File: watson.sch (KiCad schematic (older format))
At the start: 44 parts, among them P1 CONN_1, P2 CONN_1, P3 CONN_1, P4 CONN_1, P5 BNC, P6 CONN_1, U1 78L05, U2 79L05, U4 AD603, U5 AD8307

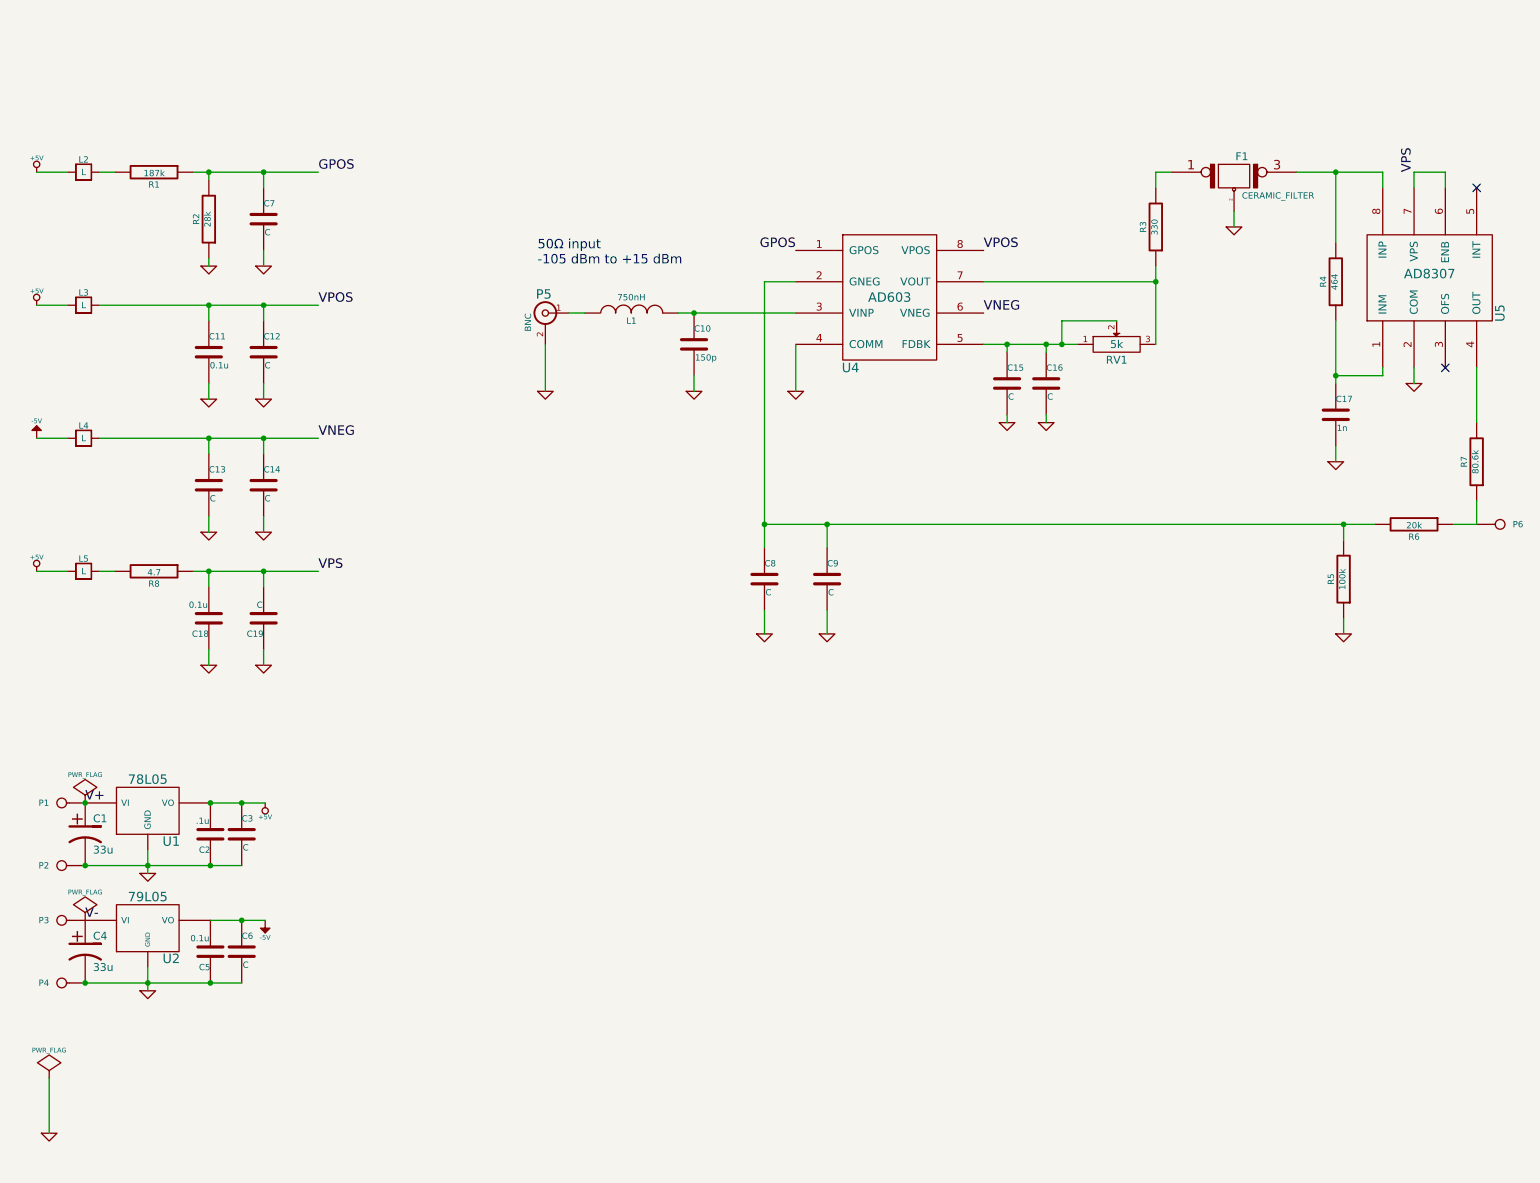
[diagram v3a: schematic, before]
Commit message: Added AD8031 to buffer output of AD8307.
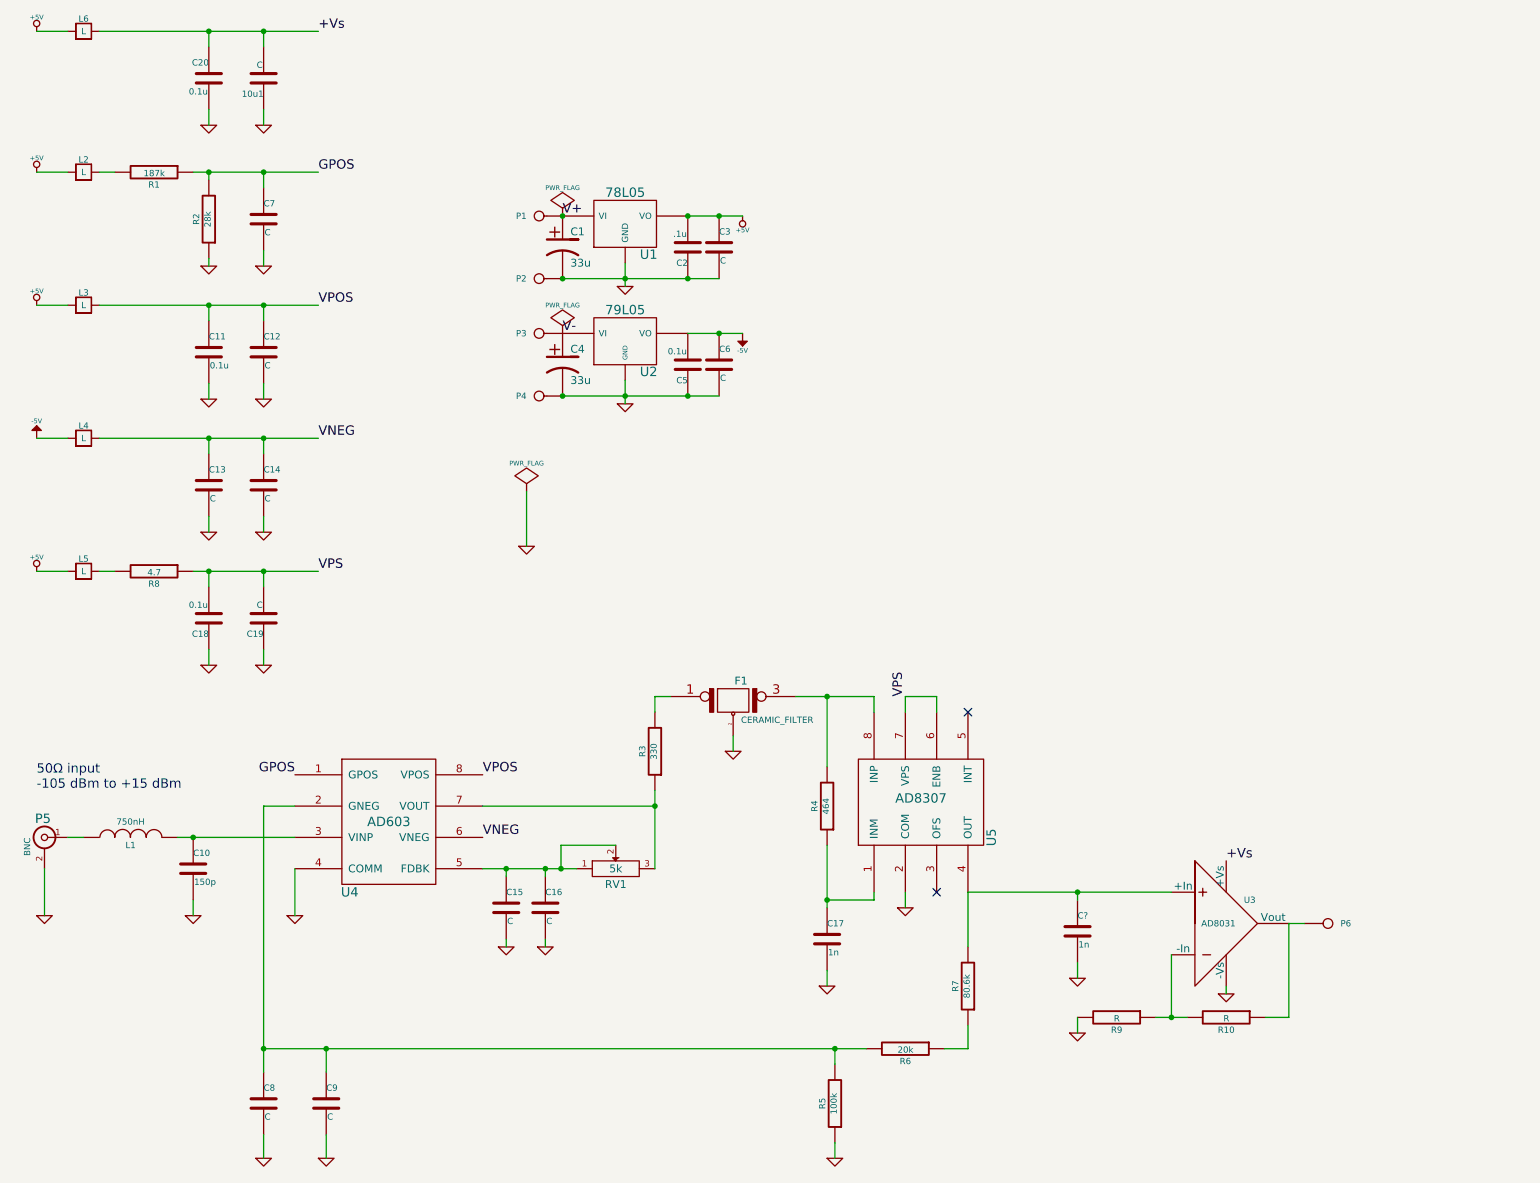
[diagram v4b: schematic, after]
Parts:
- added 10u1: C, ~, symbol C
- added C20: 0.1u, ~, symbol C
- added C?: 1n, ~, symbol C
- added L6: L, ~, symbol L
- added R10, R9: R, ~, symbol R
- added U3: AD8031, ~, symbol AD8031
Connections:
- net +5V: now also L6.1
- net GND: now also 10u1.1, C20.2, C?.2, R9.2, U3.2 (-Vs)
- net at R7.2, U5.4 (OUT): now also C?.1, U3.3 (+In)
- net at R6.1, R7.1: no longer P6.1
- new net: P6.1, R10.1, U3.1 (Vout)
- new net: R10.2, R9.1, U3.4 (-In)
- new net +Vs: 10u1.2, C20.1, L6.2, U3.5 (+Vs)
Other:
- moved on the sheet: C1, C10, C15, C16, C17, C2, C3, C4, C5, C6, C8, C9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

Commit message: This is the initial manufactured version of Watson, Watson 10 to be exact.
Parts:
- removed 10u1: C, ~, symbol C
- added C21: Spare, ~, symbol C
- C12, C14, C19, C7: value C -> Spare
- gave numbers to parts that had none: 1
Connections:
- net +Vs: now also C21.1
- net GND: now also C18.2, C19.2, C21.2; no longer C18.1, C19.1
- net VPS: now also C18.1, C19.1; no longer C18.2, C19.2
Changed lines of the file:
@@
-EESchema Schematic File Version 2  date Sunday, September 29, 2013 01:00:13 PM
+EESchema Schematic File Version 2  date Thursday, October 03, 2013 09:14:34 PM
 LIBS:watson
 LIBS:watson-cache
@@
 Sheet 1 1
 Title "Watson - A 10.7 MHz Power Meter"
-Date "29 sep 2013"
+Date "4 oct 2013"
 Rev "A"
 Comp "Copyright 2013 - Pare Technologies"
@@
 F 3 "~" H 1950 3650 60  0000 C CNN
 	1    1950 3650
-	-1   0    0    1
+	1    0    0    -1
 $EndComp
 $Comp
@@
 P 2300 2800
 F 0 "C14" H 2300 2900 40  0000 L CNN
-F 1 "C" H 2306 2715 40  0000 L CNN
+F 1 "Spare" H 2306 2715 40  0000 L CNN
 F 2 "~" H 2338 2650 30  0000 C CNN
 F 3 "~" H 2300 2800 60  0000 C CNN
@@
 P 2300 1950
 F 0 "C12" H 2300 2050 40  0000 L CNN
-F 1 "C" H 2306 1865 40  0000 L CNN
+F 1 "Spare" H 2306 1865 40  0000 L CNN
 F 2 "~" H 2338 1800 30  0000 C CNN
 F 3 "~" H 2300 1950 60  0000 C CNN
@@
 P 2300 3650
 F 0 "C19" H 2300 3750 40  0000 L CNN
-F 1 "C" H 2306 3565 40  0000 L CNN
+F 1 "Spare" H 2306 3565 40  0000 L CNN
 F 2 "~" H 2338 3500 30  0000 C CNN
 F 3 "~" H 2300 3650 60  0000 C CNN
 	1    2300 3650
-	-1   0    0    1
+	1    0    0    -1
 $EndComp
 $Comp
@@
 P 2300 1100
 F 0 "C7" H 2300 1200 40  0000 L CNN
-F 1 "C" H 2306 1015 40  0000 L CNN
+F 1 "Spare" H 2306 1015 40  0000 L CNN
 F 2 "~" H 2338 950 30  0000 C CNN
 F 3 "~" H 2300 1100 60  0000 C CNN
@@
 	3980 2840 3980 3190
 Wire Wire Line
-	4610 1380 4610 1480
-Wire Wire Line
-	4610 1480 4610 1530
-Wire Wire Line
-	4610 2130 4610 2230
-Wire Wire Line
-	4610 2230 4610 2280
+	4610 1380 4610 1530
+Wire Wire Line
+	4610 2130 4610 2280
 Wire Wire Line
 	4210 1830 4210 1830
 Connection ~ 4610 1480
 Wire Wire Line
-	4210 2230 4610 2230
-Wire Wire Line
-	4610 2230 5010 2230
-Wire Wire Line
-	5010 2230 5210 2230
+	4210 2230 5210 2230
 Connection ~ 4610 2230
 Connection ~ 5010 1080
@@
 Connection ~ 5010 1480
 Wire Wire Line
-	4210 1480 4610 1480
-Wire Wire Line
-	4610 1480 5010 1480
-Wire Wire Line
-	5010 1480 5210 1480
+	4210 1480 5210 1480
 Connection ~ 5010 2230
 Wire Wire Line
-	5010 1080 5210 1080
-Wire Wire Line
-	5210 1080 5360 1080
+	5010 1080 5360 1080
 Connection ~ 5210 1080
 Wire Wire Line
-	5010 1830 5210 1830
-Wire Wire Line
-	5210 1830 5360 1830
+	5010 1830 5360 1830
 Connection ~ 5210 1830
 Wire Wire Line
 	3700 4850 4800 4850
 Wire Wire Line
-	4800 4750 4800 4850
-Wire Wire Line
-	4800 4850 4800 5250
+	4800 4750 4800 5250
 $Comp
 L GND #PWR027
@@
 	4100 5700 4100 5750
 Wire Wire Line
-	3700 5250 3850 5250
-Wire Wire Line
-	3850 5250 4100 5250
-Wire Wire Line
-	4100 5250 4200 5250
-Wire Wire Line
-	4200 5250 4300 5250
+	3700 5250 4300 5250
 Wire Wire Line
 	3850 5300 3850 5250
@@
 	1850 5450 1850 5550
 Wire Wire Line
-	1750 5050 1850 5050
-Wire Wire Line
-	1850 5050 2500 5050
+	1750 5050 2500 5050
 Wire Wire Line
 	1050 5050 1150 5050
@@
 	5950 7000 5950 7100
 Wire Wire Line
-	2300 4850 2300 6400
-Wire Wire Line
-	2300 6400 2300 6550
+	2300 4850 2300 6550
 Wire Wire Line
 	2300 4850 2500 4850
@@
 	5900 5900 5900 6000
 Wire Wire Line
-	5900 5100 5900 5450
-Wire Wire Line
-	5900 5450 5900 5500
+	5900 5100 5900 5500
 Wire Wire Line
 	5900 5450 6200 5450
@@
 	5900 4600 5900 4150
 Wire Wire Line
-	5700 4150 5900 4150
-Wire Wire Line
-	5900 4150 6200 4150
+	5700 4150 6200 4150
 Wire Wire Line
 	6200 4150 6200 4250
@@
 Connection ~ 5950 6400
 Wire Wire Line
-	2300 6400 2700 6400
-Wire Wire Line
-	2700 6400 5950 6400
-Wire Wire Line
-	5950 6400 6150 6400
+	2300 6400 6150 6400
 Connection ~ 2700 6400
 Wire Wire Line
-	1850 800  1950 800
-Wire Wire Line
-	1950 800  2300 800
-Wire Wire Line
-	2300 800  2650 800
+	1850 800  2650 800
 Wire Wire Line
 	1950 850  1950 800
@@
 	850  1650 1050 1650
 Wire Wire Line
-	1250 1650 1950 1650
-Wire Wire Line
-	1950 1650 2300 1650
-Wire Wire Line
-	2300 1650 2650 1650
+	1250 1650 2650 1650
 Wire Wire Line
 	1950 1750 1950 1650
@@
 	850  2500 1050 2500
 Wire Wire Line
-	1250 2500 1950 2500
-Wire Wire Line
-	1950 2500 2300 2500
-Wire Wire Line
-	2300 2500 2650 2500
+	1250 2500 2650 2500
 Wire Wire Line
 	1950 2600 1950 2500
@@
 	1250 3350 1350 3350
 Wire Wire Line
-	1850 3350 1950 3350
-Wire Wire Line
-	1950 3350 2300 3350
-Wire Wire Line
-	2300 3350 2650 3350
+	1850 3350 2650 3350
 Wire Wire Line
 	1950 3450 1950 3350
@@
 $EndComp
 Wire Wire Line
-	6800 5400 7500 5400
-Wire Wire Line
-	7500 5400 8100 5400
-Wire Wire Line
-	8000 6200 8100 6200
-Wire Wire Line
-	8100 6200 8200 6200
+	6800 5400 8100 5400
+Wire Wire Line
+	8000 6200 8200 6200
 Wire Wire Line
 	8100 6200 8100 5800
@@
 F 3 "~" H 1950 200 60  0000 C CNN
 	1    1950 200
-	-1   0    0    -1
+	1    0    0    -1
 $EndComp
 $Comp
@@
 	1    850  -100
 	1    0    0    -1
-$EndComp
-$Comp
-L C 10u1
-U 1 1 52485F4A
-P 2300 200
-F 0 "10u1" H 2300 300 40  0000 L CNN
-F 1 "C" H 2306 115 40  0000 L CNN
-F 2 "~" H 2338 50  30  0000 C CNN
-F 3 "~" H 2300 200 60  0000 C CNN
-	1    2300 200
-	-1   0    0    1
 $EndComp
 $Comp
@@
 	850  -100 1050 -100
 Wire Wire Line
-	1250 -100 1950 -100
-Wire Wire Line
-	1950 -100 2300 -100
-Wire Wire Line
-	2300 -100 2650 -100
+	1250 -100 2650 -100
 Wire Wire Line
 	1950 0    1950 -100
@@
 +Vs
 $Comp
-L C C?
+L C C22
 U 1 1 524863F5
 P 7500 5650
-F 0 "C?" H 7500 5750 40  0000 L CNN
+F 0 "C22" H 7500 5750 40  0000 L CNN
 F 1 "1n" H 7506 5565 40  0000 L CNN
 F 2 "~" H 7538 5500 30  0000 C CNN
@@
 $EndComp
 $Comp
-L GND #PWR?
+L GND #PWR037
 U 1 1 524863FB
 P 7500 5950
-F 0 "#PWR?" H 7500 5950 30  0001 C CNN
+F 0 "#PWR037" H 7500 5950 30  0001 C CNN
 F 1 "GND" H 7500 5880 30  0001 C CNN
 F 2 "" H 7500 5950 60  0000 C CNN
@@
 	7500 5450 7500 5400
 Connection ~ 7500 5400
+$Comp
+L C C21
+U 1 1 524B81FB
+P 2300 200
+F 0 "C21" H 2300 300 40  0000 L CNN
+F 1 "Spare" H 2306 115 40  0000 L CNN
+F 2 "~" H 2338 50  30  0000 C CNN
+F 3 "~" H 2300 200 60  0000 C CNN
+	1    2300 200
+	1    0    0    -1
+$EndComp
 $EndSCHEMATC
